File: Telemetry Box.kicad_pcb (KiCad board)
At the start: 4 copper layers, 38.1 x 41.6 mm, 74 parts, among them J1 USB_C_Receptacle, J2 DC 5V In, J3 Conn_01x06, J4 Thermistor Molex, J6 Thermistor Molex, J8 SMA, Q1 MMBT2222A-TP, SW2 SW_Push, SW3 SW_SPDT, U1 AP2112K-1.8, U10 MAX-M10S, U2 TPS62160DSG, U3 STM32F373CCTx, U4 LSM6DSRXTR, U5 MCP6L01x-xLT, U7 BMP585, U8 MCP6L01x-xLT, X1 32.768kHz

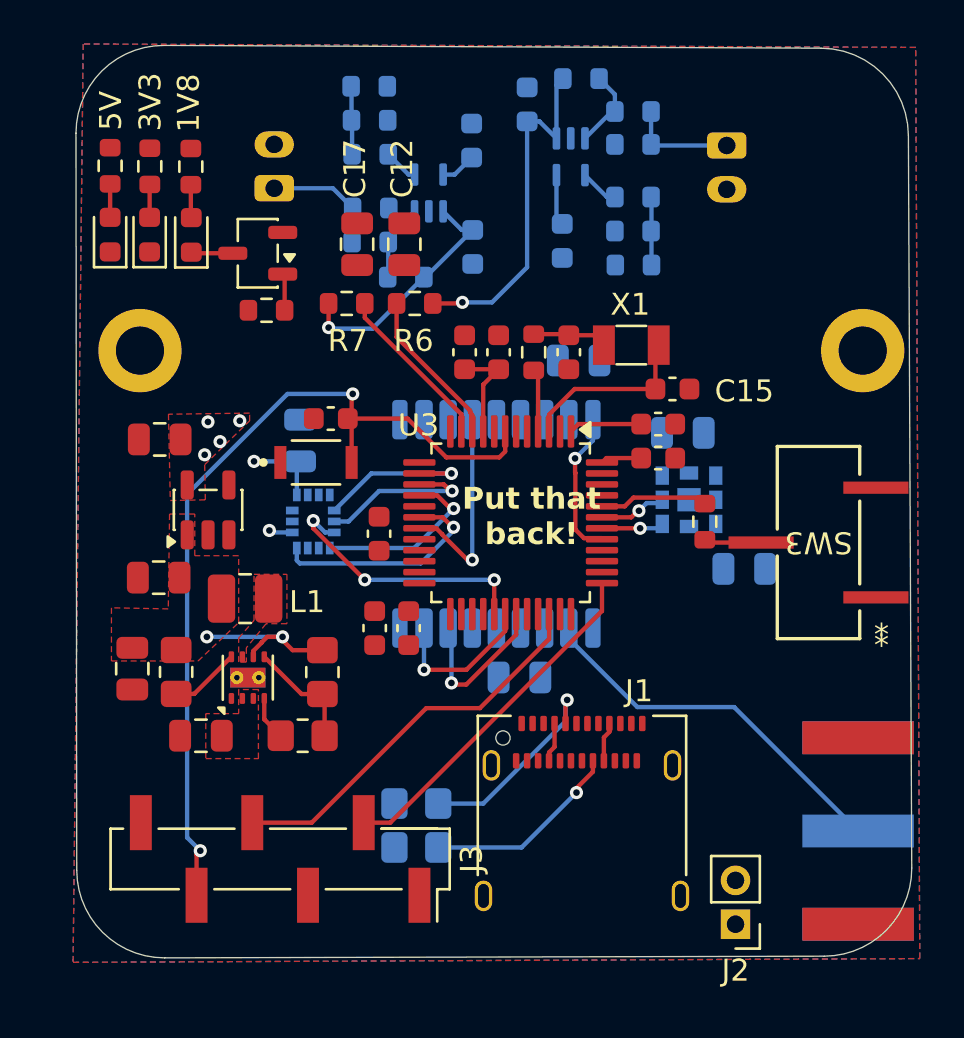
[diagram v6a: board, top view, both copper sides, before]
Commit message: Completed power routing for Rev0
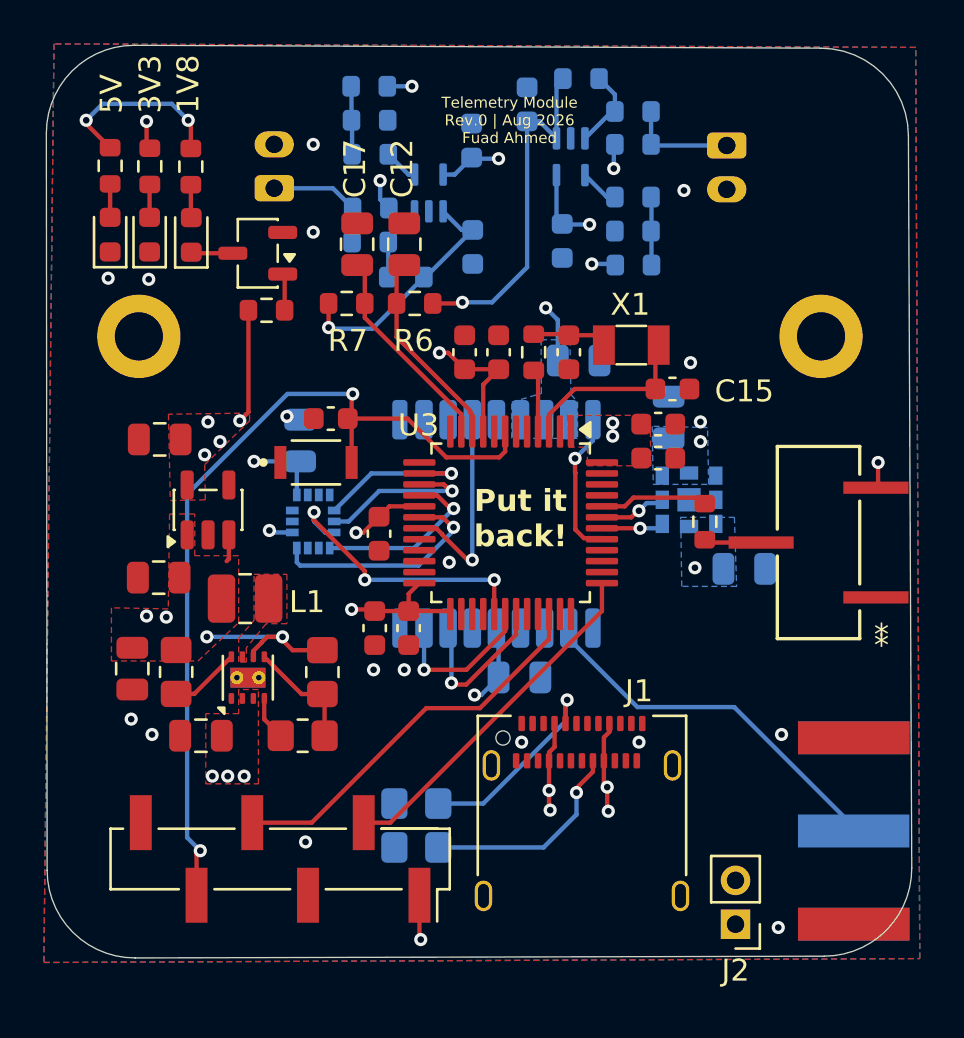
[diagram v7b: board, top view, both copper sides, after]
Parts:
- moved H1 2.01 mm to (168.1, 102.9)
- moved C26 0.96 mm to (161.2, 106.6), turned to 90 degrees
- moved H2 0.65 mm to (137.0, 102.9)
- moved J8 0.20 mm to (169.6, 125.5)
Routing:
- net +3V3: track 21.1 -> 46.5 mm, vias 2 -> 22
- net +5V: track 3.61 -> 23.4 mm, vias 0 -> 9
- net +1V8: track 4.77 -> 9.97 mm
- net /MCU/THERM2_ADC: track 7.66 -> 9.56 mm
- net /MCU/THERM1_ADC: track 7.27 -> 9.16 mm
- net /MCU/IMU_SDI: track 12.3 -> 13.1 mm
- net Net-(J1-CC2): track 9.10 -> 9.68 mm
- net PGND: vias 0 -> 18
- added copper zone on B.Cu, net +3V3
- added copper zone on In2.Cu, net +3V3
- added copper zone on In2.Cu, net +5V
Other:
- board size 38.1 x 41.6 mm -> 39.5 x 41.6 mm
- board text added: "Put it back!"
- board text added: "Telemetry Module Rev.0 | Aug 2026 Fuad Ahmed"
- board text removed: "Put that back!"

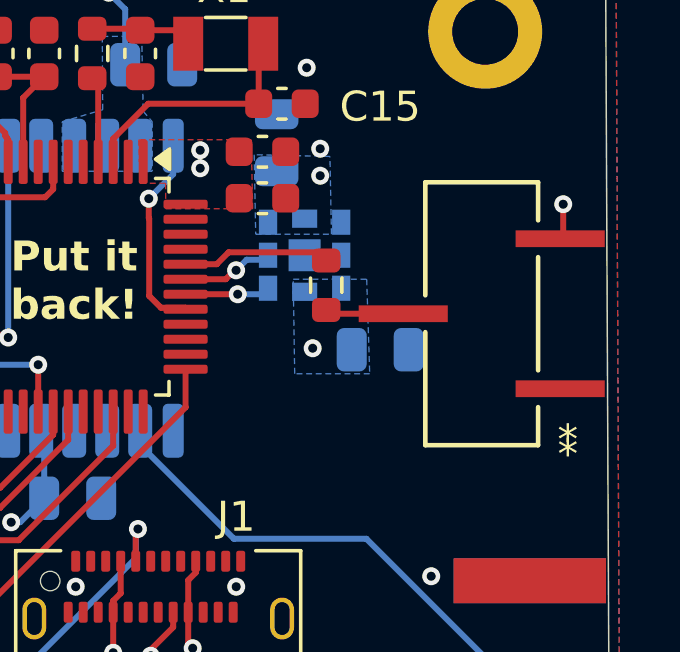
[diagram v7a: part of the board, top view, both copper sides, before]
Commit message: Updated gitignore
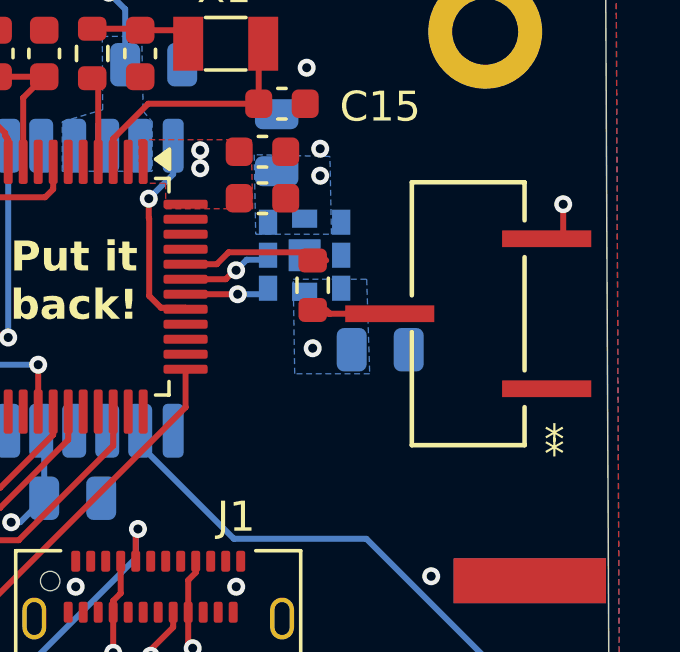
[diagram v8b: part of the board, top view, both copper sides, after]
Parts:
- moved R15 0.45 mm to (162.3, 111.3)
- moved SW3 0.45 mm to (167.5, 112.3)
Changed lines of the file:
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@@
 	(footprint "Telem_fp:SWITCH_1SCQN"
 		(layer "F.Cu")
-		(at 167.9838 112.3 180)
+		(at 167.5338 112.3 180)
 		(tags "JS102011SCQN ")
 		(property "Reference" "SW3"
@@
 	(footprint "Resistor_SMD:R_0603_1608Metric"
 		(layer "F.Cu")
-		(at 162.8 111.35 90)
+		(at 162.35 111.35 90)
 		(descr "Resistor SMD 0603 (1608 Metric), square (rectangular) end terminal, IPC-7351 nominal, (Body size source: IPC-SM-782 page 72, https://www.pcb-3d.com/wordpress/wp-content/uploads/ipc-sm-782a_amendment_1_and_2.pdf)")
 		(tags "resistor")
@@
 	)
 	(segment
-		(start 165.3676 112.3)
-		(end 162.925 112.3)
+		(start 164.9176 112.3)
+		(end 162.475 112.3)
 		(width 0.2)
 		(layer "F.Cu")
